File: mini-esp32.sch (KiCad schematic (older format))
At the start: 51 parts, among them J1 BAT, J2 USB_B_Micro, J5 Conn_01x18, J6 Conn_01x18, Q1 AO3401A, Q2 S8050, Q3 S8050, Q4 2N7002, Q5 AO3400A, Q6 AO3400A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

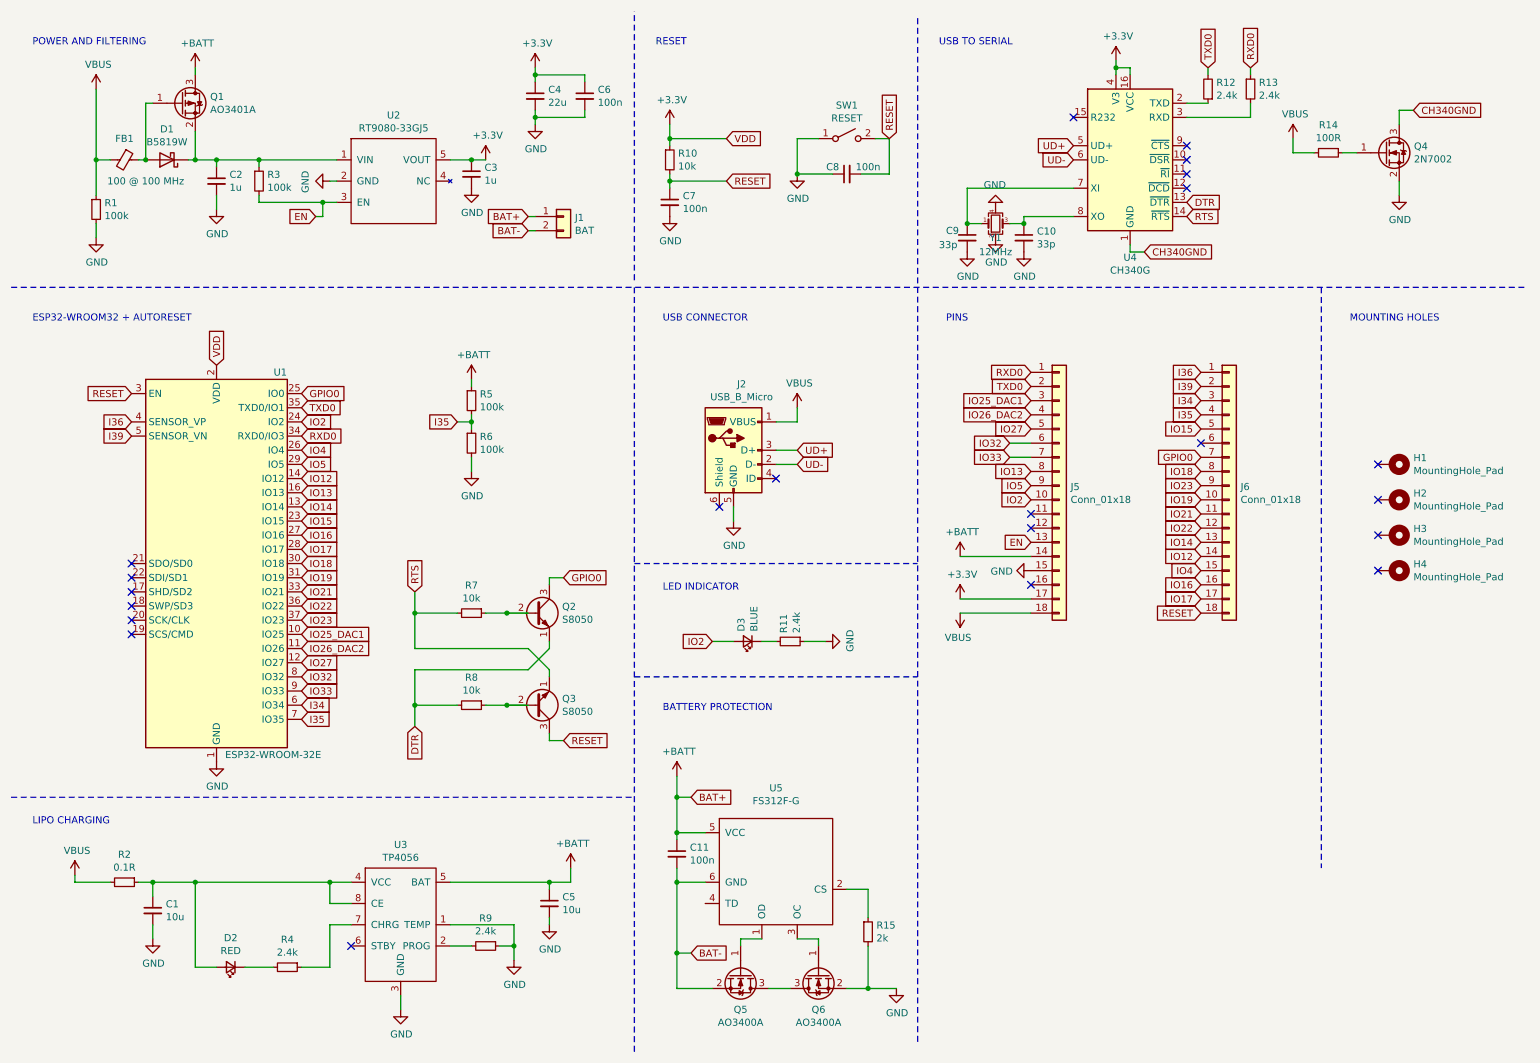
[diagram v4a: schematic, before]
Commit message: Fix three critical bugs
1. Fix RXD TXD wiring
2. Fix LDO EN pin resistor
3. Fix programming not working (DTR RTS programming transistor resistor values)
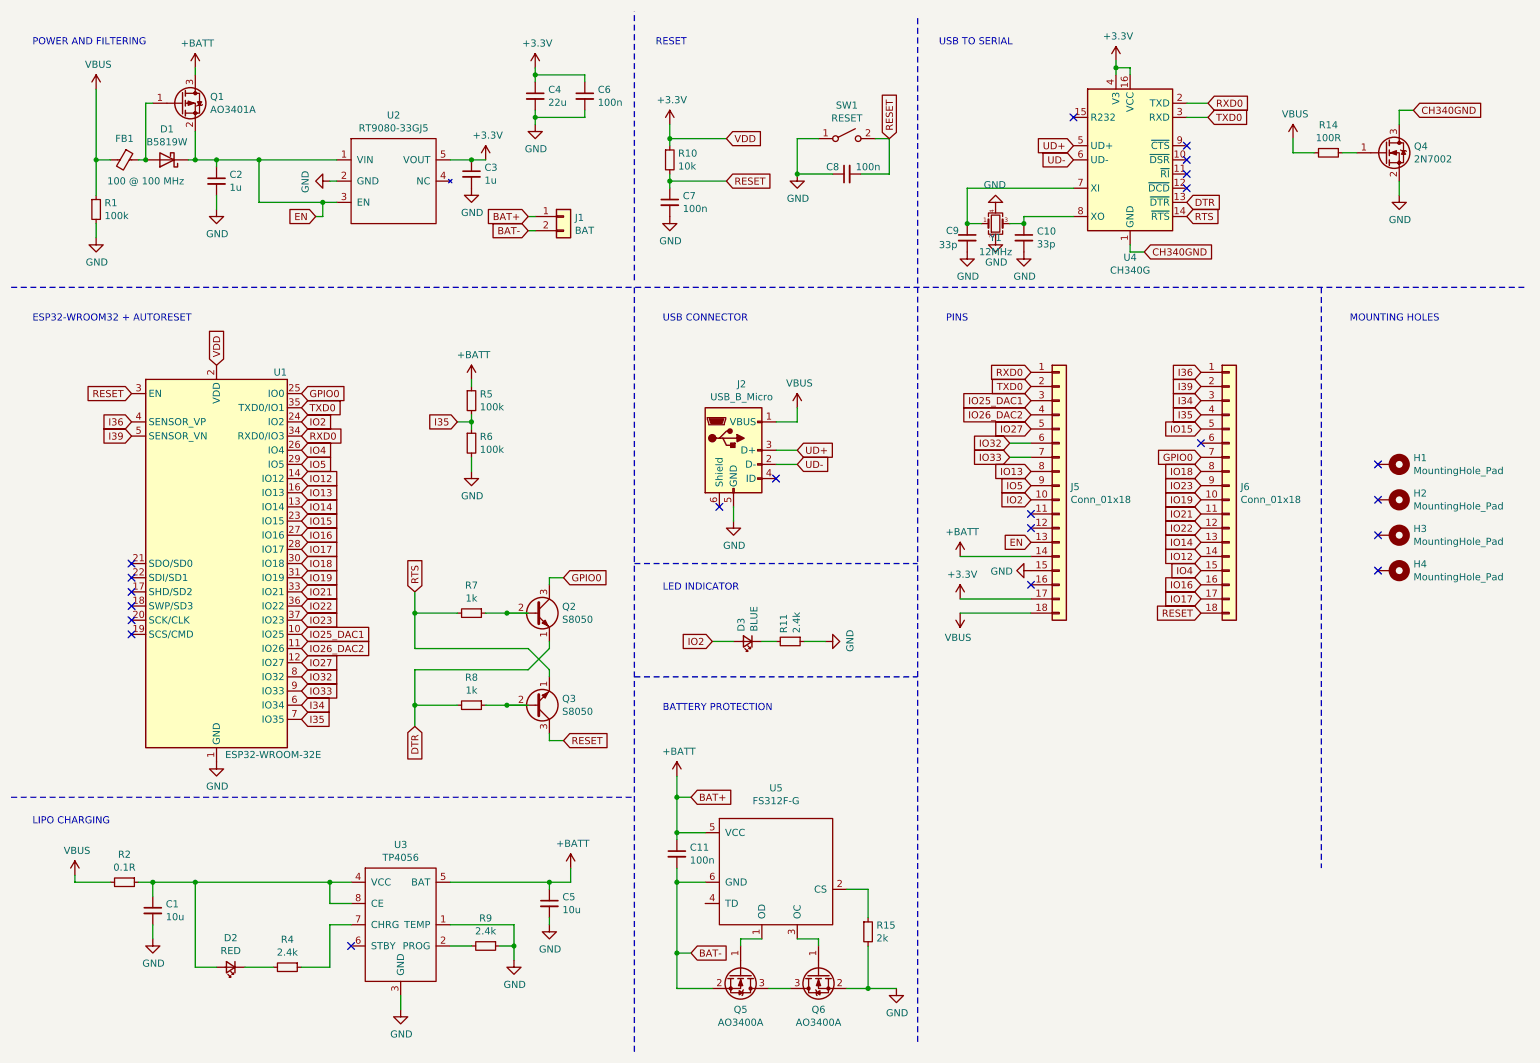
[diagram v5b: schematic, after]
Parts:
- removed R12, R13: 2.4k, Resistor_SMD:R_0402_1005Metric, symbol Device:R_Small
- removed R3: 100k, Resistor_SMD:R_0402_1005Metric, symbol Device:R_Small
- R7, R8: value 10k -> 1k; LCSC Part # C25744 -> C11702
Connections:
- net EN: now also C2.1, D1.1 (K), Q1.2 (S), U2.1 (VIN)
- net RXD0: now also U4.2 (TXD)
- net TXD0: now also U4.3 (RXD)
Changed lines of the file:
@@
 Title "Mini ESP32"
 Date "2020-10-11"
-Rev "2.0"
+Rev "3.0"
 Comp ""
 Comment1 ""
@@
 Wire Wire Line
 	1800 1500 1750 1500
-$Comp
-L Device:R_Small R3
-U 1 1 5F87DCF0
-P 2250 1650
-F 0 "R3" H 2309 1696 50  0000 L CNN
-F 1 "100k" H 2309 1605 50  0000 L CNN
-F 2 "Resistor_SMD:R_0402_1005Metric" H 2250 1650 50  0001 C CNN
-F 3 "~" H 2250 1650 50  0001 C CNN
-F 4 "C25741" H 2250 1650 50  0001 C CNN "LCSC Part #"
-	1    2250 1650
-	1    0    0    -1
-$EndComp
 Wire Wire Line
 	2750 1650 2800 1650
@@
 	2800 1500 2250 1500
 Wire Wire Line
-	2250 1550 2250 1500
-Wire Wire Line
 	2800 1800 2700 1800
-Wire Wire Line
-	2250 1800 2250 1750
 Wire Wire Line
 	1950 1500 1950 1550
@@
 P 3750 4700
 F 0 "R7" V 3554 4700 50  0000 C CNN
-F 1 "10k" V 3645 4700 50  0000 C CNN
+F 1 "1k" V 3645 4700 50  0000 C CNN
 F 2 "Resistor_SMD:R_0402_1005Metric" H 3750 4700 50  0001 C CNN
 F 3 "~" H 3750 4700 50  0001 C CNN
-F 4 "C25744" H 3750 4700 50  0001 C CNN "LCSC Part #"
+F 4 "C11702" H 3750 4700 50  0001 C CNN "LCSC Part #"
 	1    3750 4700
 	0    1    1    0
@@
 P 3750 5350
 F 0 "R8" V 3554 5350 50  0000 C CNN
-F 1 "10k" V 3645 5350 50  0000 C CNN
+F 1 "1k" V 3645 5350 50  0000 C CNN
 F 2 "Resistor_SMD:R_0402_1005Metric" H 3750 5350 50  0001 C CNN
 F 3 "~" H 3750 5350 50  0001 C CNN
-F 4 "C25744" H 3750 5350 50  0001 C CNN "LCSC Part #"
+F 4 "C11702" H 3750 5350 50  0001 C CNN "LCSC Part #"
 	1    3750 5350
 	0    1    1    0
@@
 UD-
 NoConn ~ 8000 1200
-$Comp
-L Device:R_Small R12
-U 1 1 5F962BCD
-P 8950 1000
-F 0 "R12" H 8891 954 50  0000 R CNN
-F 1 "2.4k" H 8891 1045 50  0000 R CNN
-F 2 "Resistor_SMD:R_0402_1005Metric" H 8950 1000 50  0001 C CNN
-F 3 "~" H 8950 1000 50  0001 C CNN
-F 4 "C25882" H 8950 1000 50  0001 C CNN "LCSC Part #"
-	1    8950 1000
-	-1   0    0    1
-$EndComp
-$Comp
-L Device:R_Small R13
-U 1 1 5F9631E2
-P 9250 1000
-F 0 "R13" H 9309 1046 50  0000 L CNN
-F 1 "2.4k" H 9309 955 50  0000 L CNN
-F 2 "Resistor_SMD:R_0402_1005Metric" H 9250 1000 50  0001 C CNN
-F 3 "~" H 9250 1000 50  0001 C CNN
-F 4 "C25882" H 9250 1000 50  0001 C CNN "LCSC Part #"
-	1    9250 1000
-	1    0    0    -1
-$EndComp
-Text GLabel 8950 850  1    50   Input ~ 0
+Text GLabel 8950 1200 2    50   Input ~ 0
 TXD0
-Text GLabel 9250 850  1    50   Input ~ 0
+Text GLabel 8950 1100 2    50   Input ~ 0
 RXD0
 Wire Wire Line
 	8800 1100 8950 1100
-Wire Wire Line
-	8950 900  8950 850
-Wire Wire Line
-	8800 1200 9250 1200
-Wire Wire Line
-	9250 1200 9250 1100
-Wire Wire Line
-	9250 900  9250 850
 Text GLabel 8800 1800 2    50   Input ~ 0
 DTR
@@
 Text GLabel 4150 2000 0    50   Input ~ 0
 BAT-
+Wire Wire Line
+	8800 1200 8950 1200
+Wire Wire Line
+	2250 1500 2250 1800
 $EndSCHEMATC

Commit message: Fix more critical bugs
Fix NPN transistor pin mapping.
Re-add LDO EN pin pull up resistor.
Fix battery protection IC wiring and components to recommendation.
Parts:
- added R12: 100R, Resistor_SMD:R_0402_1005Metric, symbol Device:R_Small
- added R3: 10k, Resistor_SMD:R_0402_1005Metric, symbol Device:R_Small
- Q2, Q3: symbol Transistor_BJT:S8050 -> Device:Q_NPN_BEC
- R15: value 2k -> 1k; LCSC Part # C4109 -> C11702
- R9: footprint Resistor_SMD:R_0402_1005Metric -> Resistor_SMD:R_0603_1608Metric; LCSC Part # C25882 -> C22940
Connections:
- net +BATT: now also R12.2; no longer C11.1, U5.5 (VCC)
- net DTR: now also Q2.2 (E); no longer Q2.1 (E)
- net EN: now also R3.2; no longer C2.1, D1.1 (K), Q1.2 (S), U2.1 (VIN)
- net RTS: now also Q3.2 (E); no longer Q3.1 (E)
- net at R7.1: now also Q2.1 (B); no longer Q2.2 (B)
- net at R8.1: now also Q3.1 (B); no longer Q3.2 (B)
- new net: C2.1, D1.1 (K), Q1.2 (S), R3.1, U2.1 (VIN)
- new net: C11.1, R12.1, U5.5 (VCC)
- no-connect marks 22 -> 23
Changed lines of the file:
@@
 	2750 1650 2800 1650
 Wire Wire Line
-	2800 1500 2250 1500
-Wire Wire Line
 	2800 1800 2700 1800
 Wire Wire Line
 	1950 1500 1950 1550
-Wire Wire Line
-	1950 1500 2250 1500
-Connection ~ 2250 1500
 $Comp
 L power:GND #PWR0115
@@
 Text GLabel 6700 1350 1    50   Input ~ 0
 RESET
-Wire Notes Line
-	4900 2350 4900 450
 Text Notes 650  700  0    50   ~ 0
 POWER AND FILTERING
@@
 	3750 3700 3750 3600
 $Comp
-L Transistor_BJT:S8050 Q2
+L Device:Q_NPN_BEC Q2
 U 1 1 5F8F9385
 P 4200 4700
@@
 F 1 "S8050" H 4390 4655 50  0000 L CNN
 F 2 "Package_TO_SOT_SMD:SOT-23" H 4400 4625 50  0001 L CIN
-F 3 "http://www.unisonic.com.tw/datasheet/S8050.pdf" H 4200 4700 50  0001 L CNN
+F 3 "" H 4200 4700 50  0001 L CNN
 F 4 "C2146" H 4200 4700 50  0001 C CNN "LCSC Part #"
 	1    4200 4700
@@
 $EndComp
 $Comp
-L Transistor_BJT:S8050 Q3
+L Device:Q_NPN_BEC Q3
 U 1 1 5F8FA064
 P 4200 5350
@@
 F 1 "S8050" H 4390 5395 50  0000 L CNN
 F 2 "Package_TO_SOT_SMD:SOT-23" H 4400 5275 50  0001 L CIN
-F 3 "http://www.unisonic.com.tw/datasheet/S8050.pdf" H 4200 5350 50  0001 L CNN
+F 3 "" H 4200 5350 50  0001 L CNN
 F 4 "C2146" H 4200 5350 50  0001 C CNN "LCSC Part #"
 	1    4200 5350
@@
 	3350 4700 3650 4700
 Wire Wire Line
-	3850 4700 4000 4700
-Wire Wire Line
 	3350 5500 3350 5350
 Wire Wire Line
@@
 Wire Wire Line
 	4300 4950 4300 4900
-Wire Wire Line
-	3850 5350 4000 5350
 Text GLabel 4400 4450 2    50   Input ~ 0
 GPIO0
@@
 Wire Notes Line
 	500  2400 11200 2400
-Connection ~ 4000 4700
-Wire Wire Line
-	4000 4700 4150 4700
-Connection ~ 4000 5350
-Wire Wire Line
-	4000 5350 4150 5350
 Wire Wire Line
 	3350 4950 4150 4950
@@
 F 0 "R9" V 3654 7050 50  0000 C CNN
 F 1 "2.4k" V 3745 7050 50  0000 C CNN
-F 2 "Resistor_SMD:R_0402_1005Metric" H 3850 7050 50  0001 C CNN
+F 2 "Resistor_SMD:R_0603_1608Metric" H 3850 7050 50  0001 C CNN
 F 3 "~" H 3850 7050 50  0001 C CNN
-F 4 "C25882" H 3850 7050 50  0001 C CNN "LCSC Part #"
+F 4 "C22940" H 3850 7050 50  0001 C CNN "LCSC Part #"
 	1    3850 7050
 	0    1    1    0
@@
 Text Notes 650  6200 0    50   ~ 0
 LIPO CHARGING
-Wire Notes Line
-	4900 2400 4900 7800
 Text Notes 5100 4550 0    50   ~ 0
 LED INDICATOR
@@
 L power:+BATT #PWR0107
 U 1 1 5FBE7D4B
-P 5200 5850
-F 0 "#PWR0107" H 5200 5700 50  0001 C CNN
-F 1 "+BATT" H 5215 6023 50  0000 C CNN
-F 2 "" H 5200 5850 50  0001 C CNN
-F 3 "" H 5200 5850 50  0001 C CNN
-	1    5200 5850
+P 5200 5800
+F 0 "#PWR0107" H 5200 5650 50  0001 C CNN
+F 1 "+BATT" H 5215 5973 50  0000 C CNN
+F 2 "" H 5200 5800 50  0001 C CNN
+F 3 "" H 5200 5800 50  0001 C CNN
+	1    5200 5800
 	1    0    0    -1
 $EndComp
@@
 P 6550 6950
 F 0 "R15" H 6609 6996 50  0000 L CNN
-F 1 "2k" H 6609 6905 50  0000 L CNN
+F 1 "1k" H 6609 6905 50  0000 L CNN
 F 2 "Resistor_SMD:R_0402_1005Metric" H 6550 6950 50  0001 C CNN
 F 3 "~" H 6550 6950 50  0001 C CNN
-F 4 "C4109" H 6550 6950 50  0001 C CNN "LCSC Part #"
+F 4 "C11702" H 6550 6950 50  0001 C CNN "LCSC Part #"
 	1    6550 6950
 	1    0    0    -1
@@
 Wire Wire Line
 	4150 1900 4200 1900
-Wire Wire Line
-	5400 6250 5200 6250
-Connection ~ 5200 6250
-Wire Wire Line
-	5200 6250 5200 6000
-Text GLabel 5300 6000 2    50   Input ~ 0
+Text GLabel 5300 5900 2    50   Input ~ 0
 BAT+
 Wire Wire Line
-	5300 6000 5200 6000
-Connection ~ 5200 6000
-Wire Wire Line
-	5200 6000 5200 5850
+	5300 5900 5200 5900
+Wire Wire Line
+	5200 5900 5200 5800
 Text GLabel 5300 7100 2    50   Input ~ 0
 BAT-
@@
 	8800 1200 8950 1200
 Wire Wire Line
-	2250 1500 2250 1800
+	1950 1500 2250 1500
+$Comp
+L Device:R_Small R3
+U 1 1 5FB3AA5C
+P 2250 1650
+F 0 "R3" H 2309 1696 50  0000 L CNN
+F 1 "10k" H 2309 1605 50  0000 L CNN
+F 2 "Resistor_SMD:R_0402_1005Metric" H 2250 1650 50  0001 C CNN
+F 3 "~" H 2250 1650 50  0001 C CNN
+F 4 "C25744" H 2250 1650 50  0001 C CNN "LCSC Part #"
+	1    2250 1650
+	1    0    0    -1
+$EndComp
+Wire Wire Line
+	2250 1550 2250 1500
+Connection ~ 2250 1500
+Wire Wire Line
+	2250 1500 2800 1500
+Wire Wire Line
+	2250 1750 2250 1800
+Wire Wire Line
+	3850 5350 4000 5350
+Wire Wire Line
+	3850 4700 4000 4700
+NoConn ~ 5400 6750
+$Comp
+L Device:R_Small R12
+U 1 1 5FBAC8E8
+P 5200 6100
+F 0 "R12" V 5004 6100 50  0000 C CNN
+F 1 "100R" V 5095 6100 50  0000 C CNN
+F 2 "Resistor_SMD:R_0402_1005Metric" H 5200 6100 50  0001 C CNN
+F 3 "~" H 5200 6100 50  0001 C CNN
+F 4 "C25076" H 5200 6100 50  0001 C CNN "LCSC Part #"
+	1    5200 6100
+	1    0    0    1
+$EndComp
+Wire Wire Line
+	5200 5900 5200 6000
+Connection ~ 5200 5900
+Wire Notes Line
+	4900 500  4900 7800
+Wire Wire Line
+	5400 6250 5200 6250
+Connection ~ 5200 6250
+Wire Wire Line
+	5200 6250 5200 6200
 $EndSCHEMATC
